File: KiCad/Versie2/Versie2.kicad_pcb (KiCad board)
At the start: 4 copper layers, 56.3 x 45.4 mm, 100 parts, among them IC1 AP9221SA-CC-HAC-7, IC2 ISL91107IRTNZ-T7A, J1 Micro_SD_Card_Det, J10 Screw_Terminal_01x02, J11 Screw_Terminal_01x02, J12 Conn_01x01_Male, J13 Screw_Terminal_01x02, J2 USB_C_Receptacle_USB3.0, J3 JTAG, J4 Programmer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

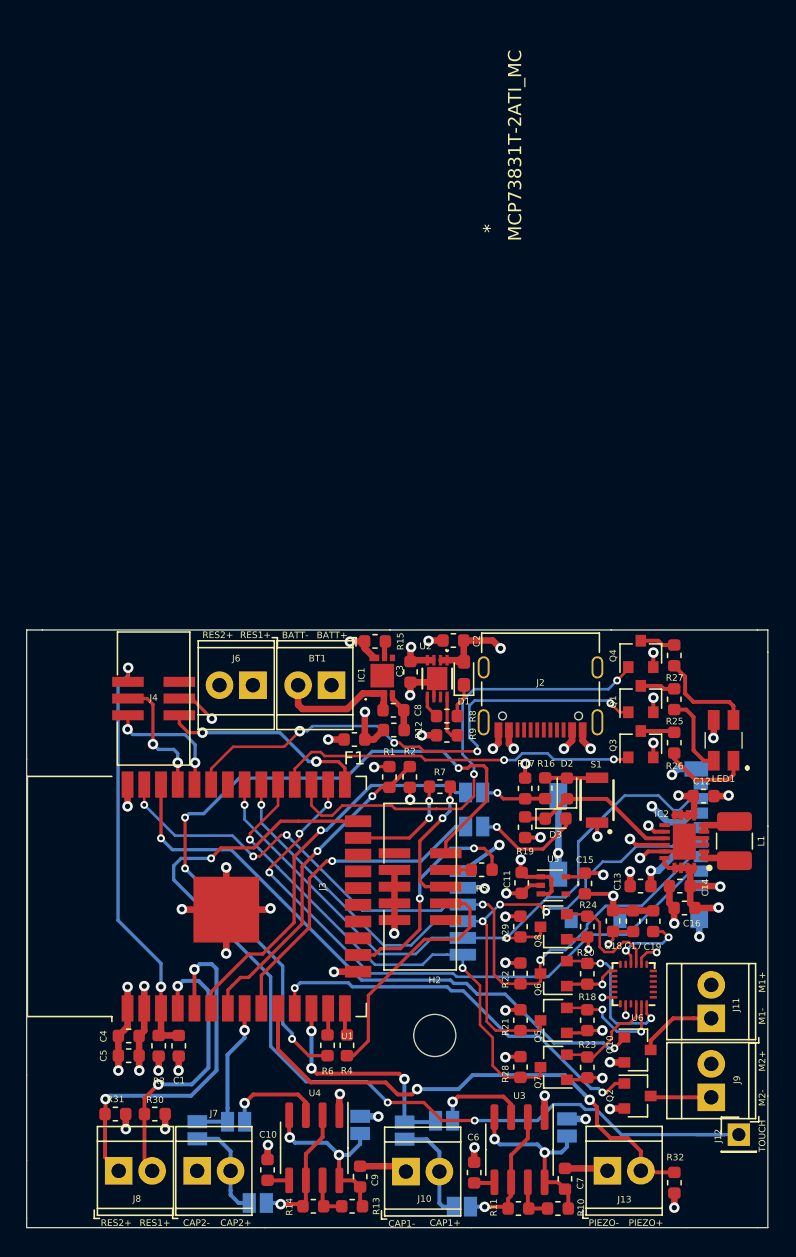
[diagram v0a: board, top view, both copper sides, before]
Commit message: Deelsystemen ingedeeld met C en H files
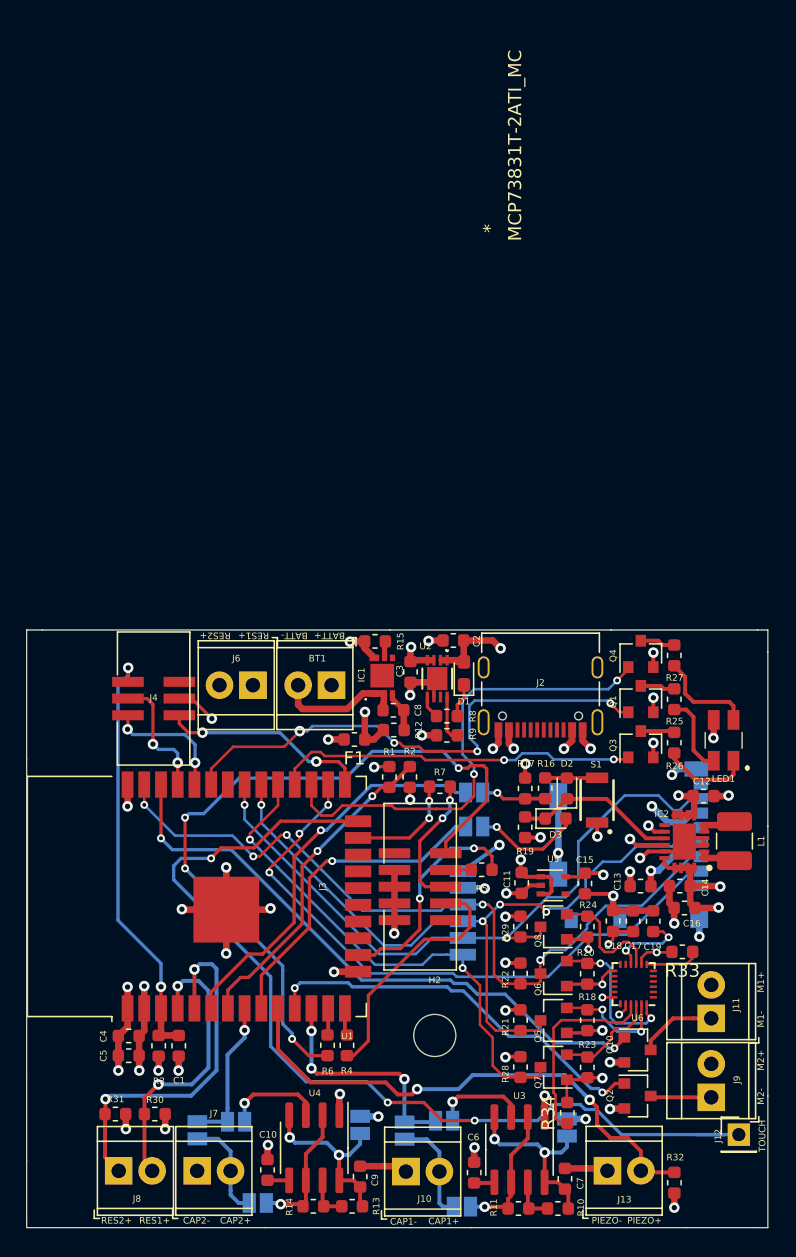
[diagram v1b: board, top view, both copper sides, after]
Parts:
- added R33: 2.2k, Resistor_SMD:R_0603_1608Metric, F.Cu at (109.7, 73.9)
- added R34: 2.2k, Resistor_SMD:R_0603_1608Metric, F.Cu at (101.0, 86.1)
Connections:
- U6 pad 21: (no net) -> Net-(R34-Pad1)
- U6 pad 7: (no net) -> Net-(R33-Pad1)
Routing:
- net Net-(R34-Pad1): track 0.00 -> 15.2 mm
- net Net-(R33-Pad1): track 0.00 -> 4.16 mm
- net +1V8: track 20.1 -> 23.0 mm
